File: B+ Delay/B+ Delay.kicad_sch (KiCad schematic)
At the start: 31 parts, among them J1 Pwr in, J2 B+ IN, J3 B+ Out, J4 LED, Q3 MMBT3904, Q4 MMBT3906, U1 LM7805_TO220, U2 SE556, U3 CPC1779

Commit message: Add files via upload
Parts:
- added U4: CPC1779, CH parts:CPC1779J, symbol Relay_SolidState:S102S01
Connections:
- net at R1.2, U3.4: now also U4.4
- net at J2.2 (Pin_2): now also U4.1; no longer J3.2 (Pin_2)
- net at Q3.3 (C), U2.10 (R), U3.3: now also U4.3
- new net: J3.2 (Pin_2), U4.2
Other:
- moved on the sheet: C6, C9, D6, J1, J2, J3, R1, U1, U3

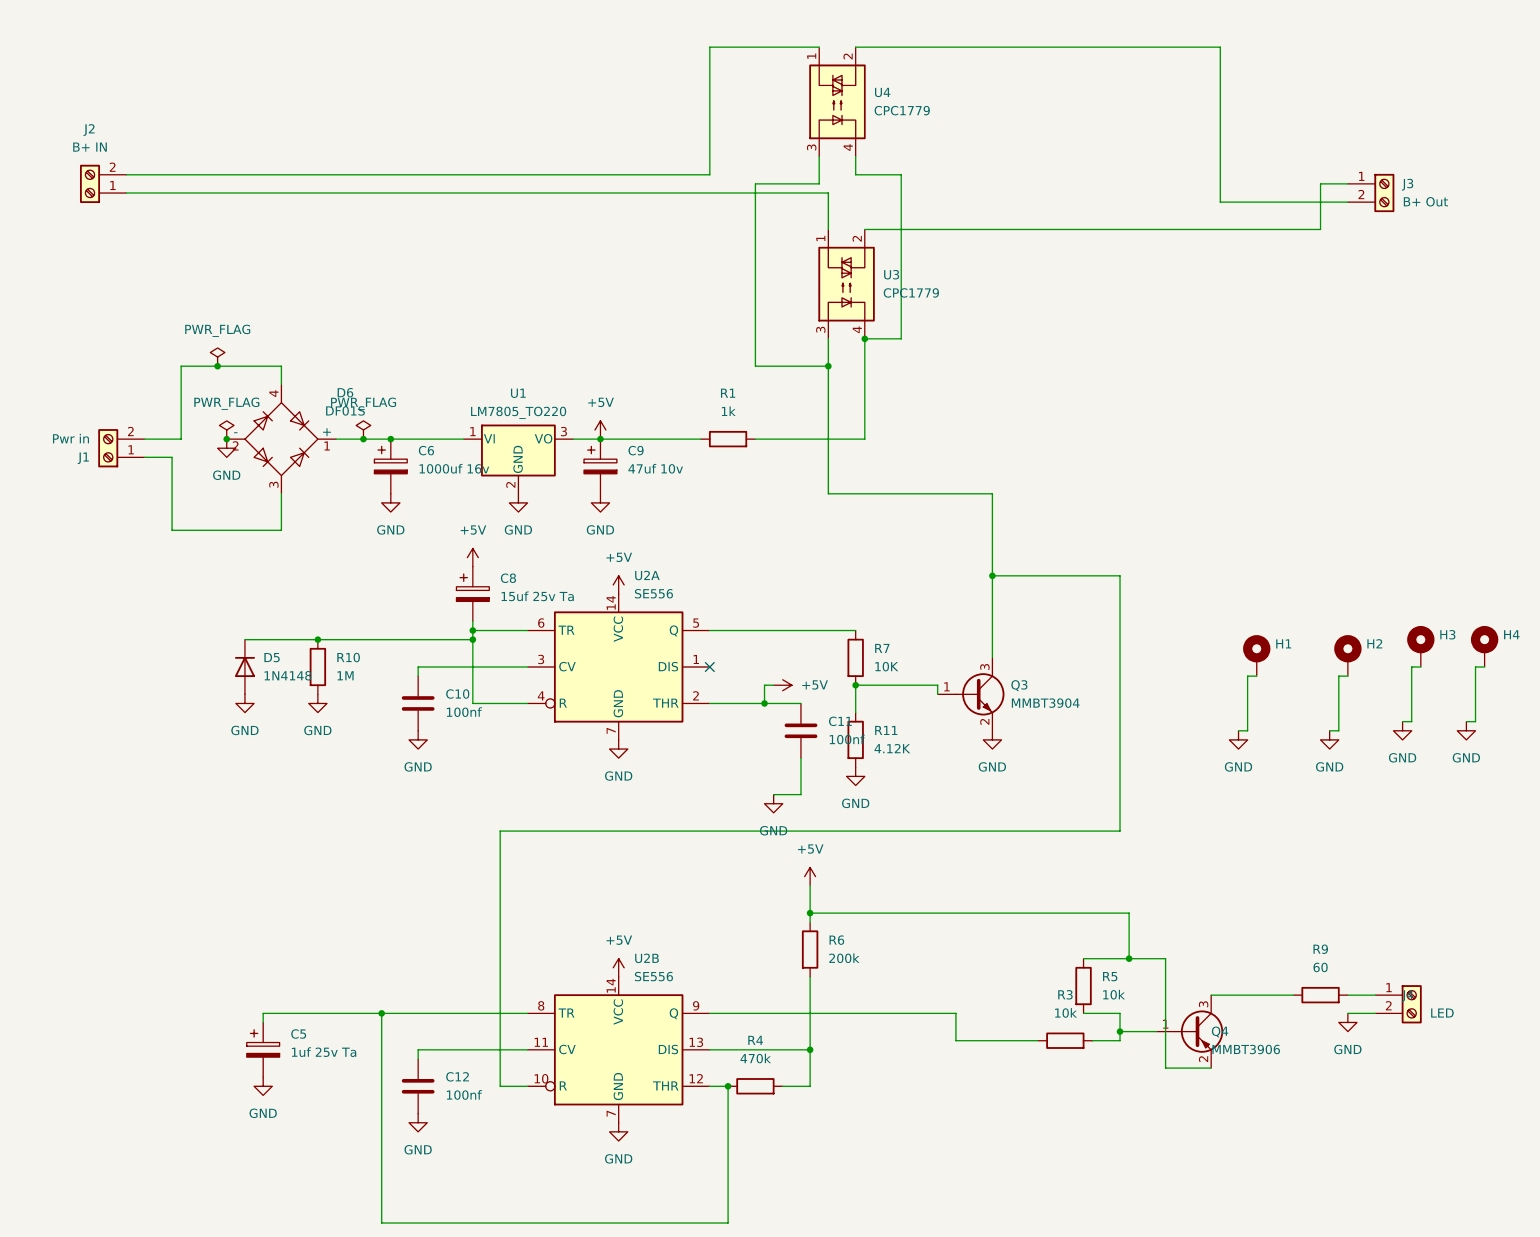
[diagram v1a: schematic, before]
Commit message: New rev, dual relay, fixed stuff
Fixing missing ground trace, correct footprint for diode, added test points, changed B++ input/output on terminal block
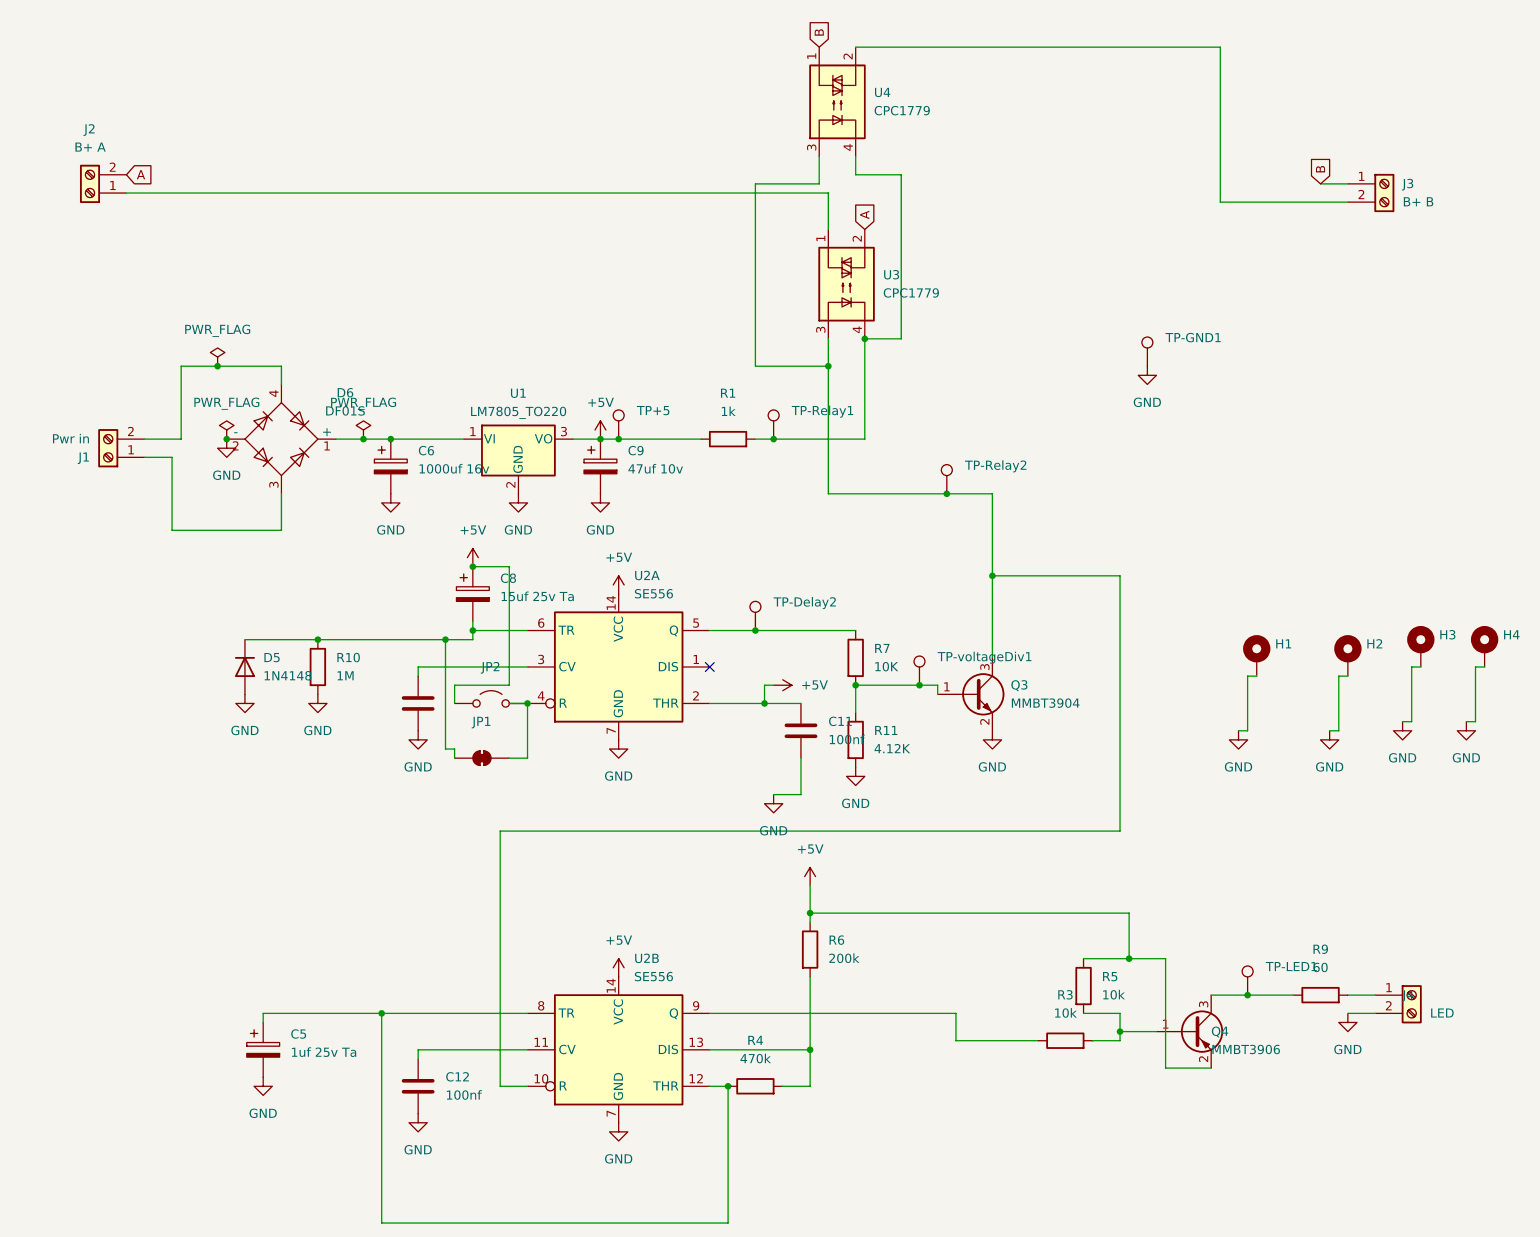
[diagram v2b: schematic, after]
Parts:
- added JP1: ~, Jumper:SolderJumper-2_P1.3mm_Bridged_RoundedPad1.0x1.5mm, symbol Jumper:SolderJumper_2_Bridged
- added JP2: ~, Jumper:SolderJumper-2_P1.3mm_Open_RoundedPad1.0x1.5mm, symbol Jumper:Jumper_2_Open
- added TP+5, TP-Delay2, TP-GND1, TP-LED1, TP-Relay1, TP-Relay2, TP-voltageDiv1: ~, TestPoint:TestPoint_Keystone_5010-5014_Multipurpose, symbol Connector:TestPoint
- D5: footprint Diode_SMD:D_0805_2012Metric_Pad1.15x1.40mm_HandSolder -> Diode_SMD:D_SOD-123
- J2: value B+ IN -> B+ A
- J3: value B+ Out -> B+ B
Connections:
- net +5V: now also JP2.1 (A), TP+5.1
- net GND: now also TP-GND1.1
- net at Q4.3 (C), R9.1: now also TP-LED1.1
- net at C8.2, D5.1 (K), R10.1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: now also JP1.1 (A); no longer U2.4 (R)
- net at R7.1, U2.5 (Q): now also TP-Delay2.1
- net at R1.2, U3.4, U4.4: now also TP-Relay1.1
- net A: now reaches J2.2 (Pin_2)
- net A: now also U3.2; no longer U4.1
- net B: now reaches J3.1 (Pin_1)
- net B: now also U4.1; no longer U3.2
- net at Q3.3 (C), U2.10 (R), U3.3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: now also TP-Relay2.1
- net at Q3.1 (B), R11.1, R7.2: now also TP-voltageDiv1.1
- new net: JP1.2 (B), JP2.2 (B), U2.4 (R)

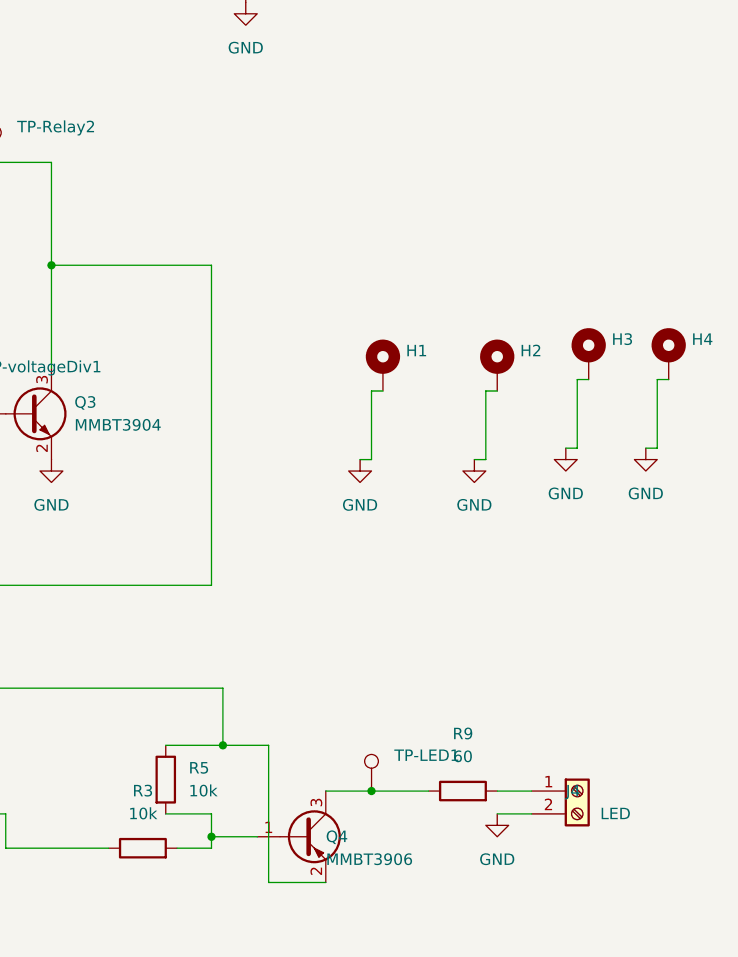
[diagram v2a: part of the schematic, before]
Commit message: Rev 5
Moved power supply parts so they don't bump SS relays, if they are bent over. Put 2nd relay so foil side is up for heatsink
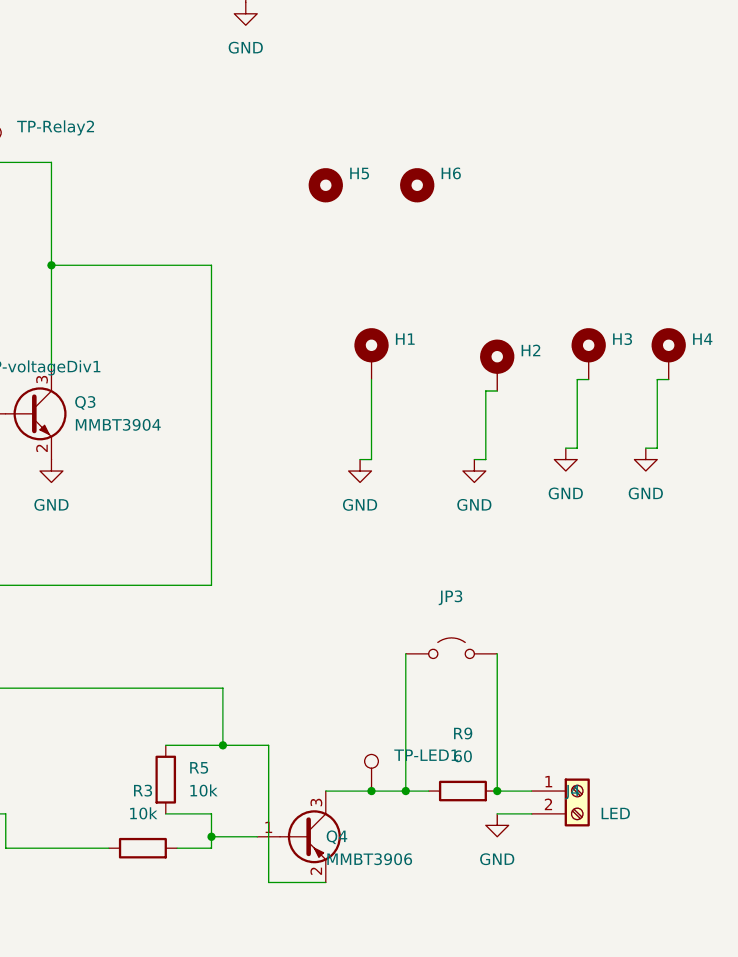
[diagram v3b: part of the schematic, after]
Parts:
- added H5: MountingHole, MountingHole:MountingHole_3.2mm_M3_Pad_TopBottom, symbol Mechanical:MountingHole
- added H6: MountingHole, MountingHole:MountingHole_3.2mm_M3_ISO14580_Pad_TopBottom, symbol Mechanical:MountingHole
- added JP3: Jumper_2_Open, Jumper:SolderJumper-2_P1.3mm_Open_RoundedPad1.0x1.5mm, symbol Jumper:Jumper_2_Open
- TP+5, TP-Delay2, TP-GND1, TP-LED1, TP-Relay1, TP-Relay2, TP-voltageDiv1: footprint TestPoint:TestPoint_Keystone_5010-5014_Multipurpose -> TestPoint:TestPoint_Keystone_5019_Miniature
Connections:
- net at Q4.3 (C), R9.1, TP-LED1.1: now also JP3.1 (A)
- net at J4.1 (Pin_1), R9.2: now also JP3.2 (B)
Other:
- moved on the sheet: H1

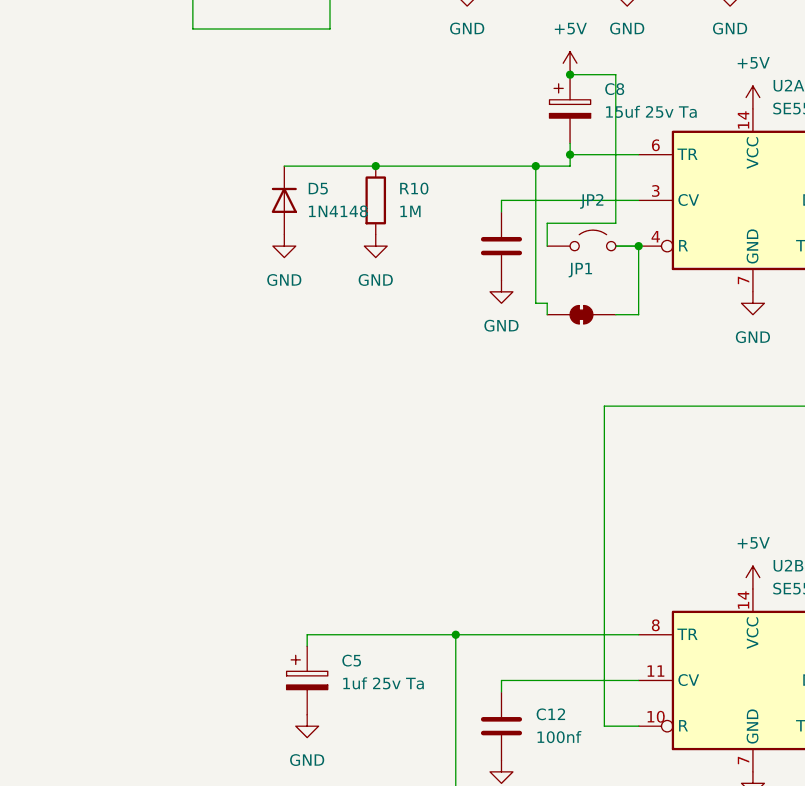
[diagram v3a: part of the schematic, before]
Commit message: Added 2 more time values w jumpers
default to 15s
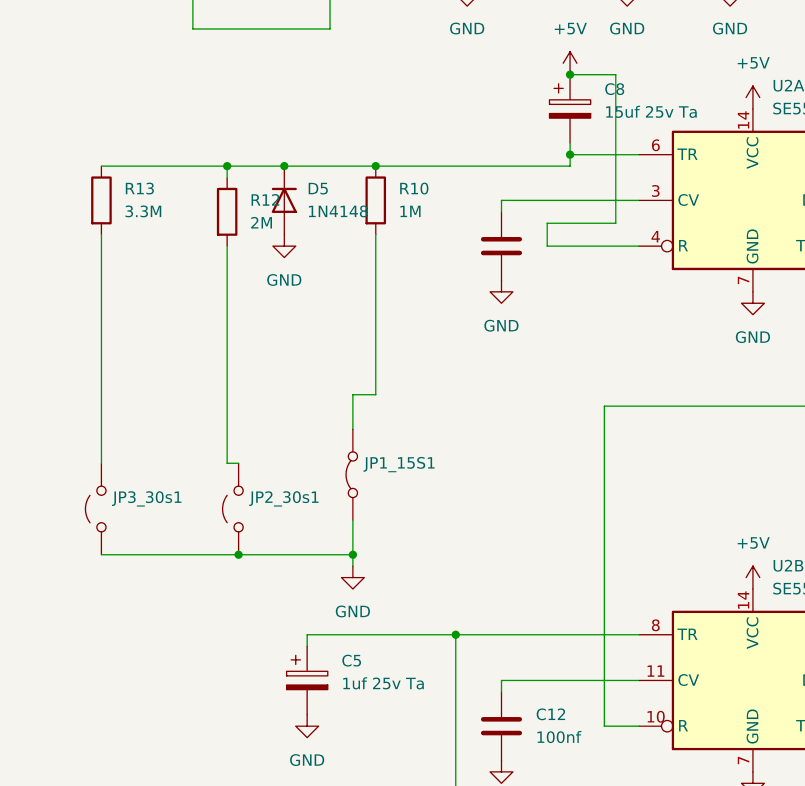
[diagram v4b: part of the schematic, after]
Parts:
- removed JP1: ~, Jumper:SolderJumper-2_P1.3mm_Bridged_RoundedPad1.0x1.5mm, symbol Jumper:SolderJumper_2_Bridged
- removed JP2: ~, Jumper:SolderJumper-2_P1.3mm_Open_RoundedPad1.0x1.5mm, symbol Jumper:Jumper_2_Open
- added JP1_15S1: Jumper_2_Bridged, Jumper:SolderJumper-2_P1.3mm_Bridged_Pad1.0x1.5mm, symbol Jumper:Jumper_2_Bridged
- added JP2_30s1, JP3_30s1: Jumper_2_Open, Jumper:SolderJumper-2_P1.3mm_Open_RoundedPad1.0x1.5mm, symbol Jumper:Jumper_2_Open
- added R12: 2M, Resistor_SMD:R_0805_2012Metric_Pad1.20x1.40mm_HandSolder, symbol Device:R
- added R13: 3.3M, Resistor_SMD:R_0805_2012Metric_Pad1.20x1.40mm_HandSolder, symbol Device:R
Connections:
- net +5V: now also U2.4 (R)
- net GND: now also JP1_15S1.1 (A), JP2_30s1.1 (A), JP3_30s1.1 (A); no longer R10.2
- net at C8.2, D5.1 (K), R10.1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: now also R12.1, R13.1
- new net: JP1_15S1.2 (B), R10.2
- new net: JP3_30s1.2 (B), R13.2
- new net: JP2_30s1.2 (B), R12.2

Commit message: Made 60s default
Jumpers for 45s and 15s
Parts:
- JP1: renamed from JP3_30s1; value Jumper_2_Open -> 15 sec
- JP2: renamed from JP2_30s1; value Jumper_2_Open -> 45s
- JP3: renamed from JP1_15S1; value Jumper_2_Bridged -> 60sec
- renumbered JP3 to JP4
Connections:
- net at JP3.2 (B): now also R13.2; no longer R10.2
- net at JP1.2 (B): now also R10.2; no longer R13.2
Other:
- moved on the sheet: JP1, JP3
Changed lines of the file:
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@@
 	(symbol
 		(lib_id "Jumper:Jumper_2_Bridged")
-		(at 55.88 134.62 90)
+		(at 27.94 138.43 90)
 		(unit 1)
 		(exclude_from_sim yes)
@@
 		(dnp no)
 		(fields_autoplaced yes)
-		(property "Reference" "JP1_15S1"
-			(at 57.15 133.3499 90)
+		(property "Reference" "JP3"
+			(at 29.21 137.1599 90)
 			(effects
 				(font
@@
 			)
 		)
-		(property "Value" "Jumper_2_Bridged"
-			(at 57.15 135.8899 90)
+		(property "Value" "60sec"
+			(at 29.21 139.6999 90)
 			(effects
 				(font
@@
 				)
 				(justify right)
-				(hide yes)
 			)
 		)
 		(property "Footprint" "Jumper:SolderJumper-2_P1.3mm_Bridged_Pad1.0x1.5mm"
-			(at 55.88 134.62 0)
+			(at 27.94 138.43 0)
 			(effects
 				(font
@@
 		)
 		(property "Datasheet" "~"
-			(at 55.88 134.62 0)
+			(at 27.94 138.43 0)
 			(effects
 				(font
@@
 		)
 		(property "Description" "Jumper, 2-pole, closed/bridged"
-			(at 55.88 134.62 0)
+			(at 27.94 138.43 0)
 			(effects
 				(font
@@
 		)
 		(instances
-			(project ""
+			(project "B+ Delay"
 				(path "/eb471509-faf7-400e-b08f-dadb99c91d71"
-					(reference "JP1_15S1")
+					(reference "JP3")
 					(unit 1)
 				)
@@
 	(symbol
 		(lib_id "Jumper:Jumper_2_Open")
-		(at 27.94 138.43 90)
+		(at 55.88 134.62 90)
 		(unit 1)
 		(exclude_from_sim yes)
@@
 		(dnp no)
 		(fields_autoplaced yes)
-		(property "Reference" "JP3_30s1"
-			(at 29.21 137.1599 90)
+		(property "Reference" "JP1"
+			(at 57.15 133.3499 90)
 			(effects
 				(font
@@
 			)
 		)
-		(property "Value" "Jumper_2_Open"
-			(at 29.21 139.6999 90)
+		(property "Value" "15 sec"
+			(at 57.15 135.8899 90)
 			(effects
 				(font
@@
 				)
 				(justify right)
-				(hide yes)
 			)
 		)
 		(property "Footprint" "Jumper:SolderJumper-2_P1.3mm_Open_RoundedPad1.0x1.5mm"
-			(at 27.94 138.43 0)
+			(at 55.88 134.62 0)
 			(effects
 				(font
@@
 		)
 		(property "Datasheet" "~"
-			(at 27.94 138.43 0)
+			(at 55.88 134.62 0)
 			(effects
 				(font
@@
 		)
 		(property "Description" "Jumper, 2-pole, open"
-			(at 27.94 138.43 0)
+			(at 55.88 134.62 0)
 			(effects
 				(font
@@
 			(project "B+ Delay"
 				(path "/eb471509-faf7-400e-b08f-dadb99c91d71"
-					(reference "JP3_30s1")
+					(reference "JP1")
 					(unit 1)
 				)
@@
 		(dnp no)
 		(fields_autoplaced yes)
-		(property "Reference" "JP2_30s1"
+		(property "Reference" "JP2"
 			(at 44.45 137.1599 90)
 			(effects
@@
 			)
 		)
-		(property "Value" "Jumper_2_Open"
+		(property "Value" "45s"
 			(at 44.45 139.6999 90)
 			(effects
@@
 				)
 				(justify right)
-				(hide yes)
 			)
 		)
@@
 			(project ""
 				(path "/eb471509-faf7-400e-b08f-dadb99c91d71"
-					(reference "JP2_30s1")
+					(reference "JP2")
 					(unit 1)
 				)
@@
 		(dnp no)
 		(fields_autoplaced yes)
-		(property "Reference" "JP3"
-			(at 196.85 128.27 0)
+		(property "Reference" "JP4"
+			(at 196.85 130.81 0)
 			(effects
 				(font
@@
 			(project ""
 				(path "/eb471509-faf7-400e-b08f-dadb99c91d71"
-					(reference "JP3")
+					(reference "JP4")
 					(unit 1)
 				)
